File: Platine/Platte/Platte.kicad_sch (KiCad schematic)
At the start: 9 parts, among them J1 Conn_01x07_MountingPin

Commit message: Plate PCB almost done
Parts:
- added J2: Conn_01x08_Socket, symbol Connector:Conn_01x08_Socket
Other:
- note added: "Mec. Stecker"
- note added: "Outputs: clock, amp_data & GNDD"
- note added: "Voltage Input: 3.3V, GNDA"
- note removed: "Outputs (6)"
- note removed: "Voltage Input"
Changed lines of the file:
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@@
+		)
+	)
+	(text "Mec. Stecker"
+		(exclude_from_sim no)
+		(at 73.406 93.726 0)
+		(effects
+			(font
+				(size 1.27 1.27)
+			)
+			(justify left bottom)
 		)
 	)
@@
 		)
 	)
-	(text "Outputs\n(6)"
-		(exclude_from_sim no)
-		(at 49.022 114.808 0)
+	(text "Outputs: clock,\namp_data & GNDD"
+		(exclude_from_sim no)
+		(at 40.132 125.476 0)
 		(effects
 			(font
@@
 		)
 	)
-	(text "Voltage\nInput"
-		(exclude_from_sim no)
-		(at 49.022 105.664 0)
+	(text "Voltage Input: \n3.3V, GNDA"
+		(exclude_from_sim no)
+		(at 45.466 96.266 0)
 		(effects
 			(font
@@
 					(unit 1)
 				)
+			)
+		)
+	)
+	(symbol
+		(lib_id "Connector:Conn_01x08_Socket")
+		(at 81.28 107.95 0)
+		(unit 1)
+		(exclude_from_sim no)
+		(in_bom yes)
+		(on_board yes)
+		(dnp no)
+		(fields_autoplaced yes)
+		(property "Reference" "J2"
+			(at 82.55 107.9499 0)
+			(effects
+				(font
+					(size 1.27 1.27)
+				)
+				(justify left)
+			)
+		)
+		(property "Value" "Conn_01x08_Socket"
+			(at 82.55 110.4899 0)
+			(effects
+				(font
+					(size 1.27 1.27)
+				)
+				(justify left)
+			)
+		)
+		(property "Footprint" ""
+			(at 81.28 107.95 0)
+			(effects
+				(font
+					(size 1.27 1.27)
+				)
+				(hide yes)
+			)
+		)
+		(property "Datasheet" "~"
+			(at 81.28 107.95 0)
+			(effects
+				(font
+					(size 1.27 1.27)
+				)
+				(hide yes)
+			)
+		)
+		(property "Description" "Generic connector, single row, 01x08, script generated"
+			(at 81.28 107.95 0)
+			(effects
+				(font
+					(size 1.27 1.27)
+				)
+				(hide yes)
+			)
+		)
+		(pin "2"
+		)
+		(pin "8"
+		)
+		(pin "4"
+		)
+		(pin "7"
+		)
+		(pin "3"
+		)
+		(pin "1"
+		)
+		(pin "6"
+		)
+		(pin "5"
+		)
+		(instances
+			(project ""
+				(path "/8ec2d373-240e-44f6-ab9e-7e8ab23831f1"
+					(reference "J2")
+					(unit 1)
+				)

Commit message: Few changes plate PCB
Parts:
- removed J1: Conn_01x07_MountingPin, Connector_JST:JST_GH_BM07B-GHS-TBT_1x07-1MP_P1.25mm_Vertical, symbol Connector_Generic_MountingPin:Conn_01x07_MountingPin
- added J1: Conn_01x08_MountingPin, Connector_JST:JST_GH_BM08B-GHS-TBT_1x08-1MP_P1.25mm_Vertical, symbol Connector_Generic_MountingPin:Conn_01x08_MountingPin
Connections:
- net +3.3V: now also J1.2 (Pin_2)
- net GNDA: now also J1.8 (Pin_8)
- net GNDD: now also J1.7 (Pin_7)
- net amp_data1: now also J1.4 (Pin_4)
- net amp_data2: now also J1.5 (Pin_5)
- net amp_data3: now also J1.6 (Pin_6)
- net out_clock: now also J1.3 (Pin_3)
- new net VCC: J1.1 (Pin_1)
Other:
- note added: "+100V"

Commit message: small changes
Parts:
- R1, R2, R3: footprint Resistor_SMD:R_01005_0402Metric_Pad0.57x0.30mm_HandSolder -> Resistor_SMD:R_0201_0603Metric_Pad0.64x0.40mm_HandSolder
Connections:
- net analog_inp_low1 is gone; now on net VCC: R1.1, U1.3 (AIN)
- net analog_inp_low2 is gone; now on net VCC: R2.1, U2.3 (AIN)
- net analog_inp_low3 is gone; now on net VCC: R3.1, U3.3 (AIN)

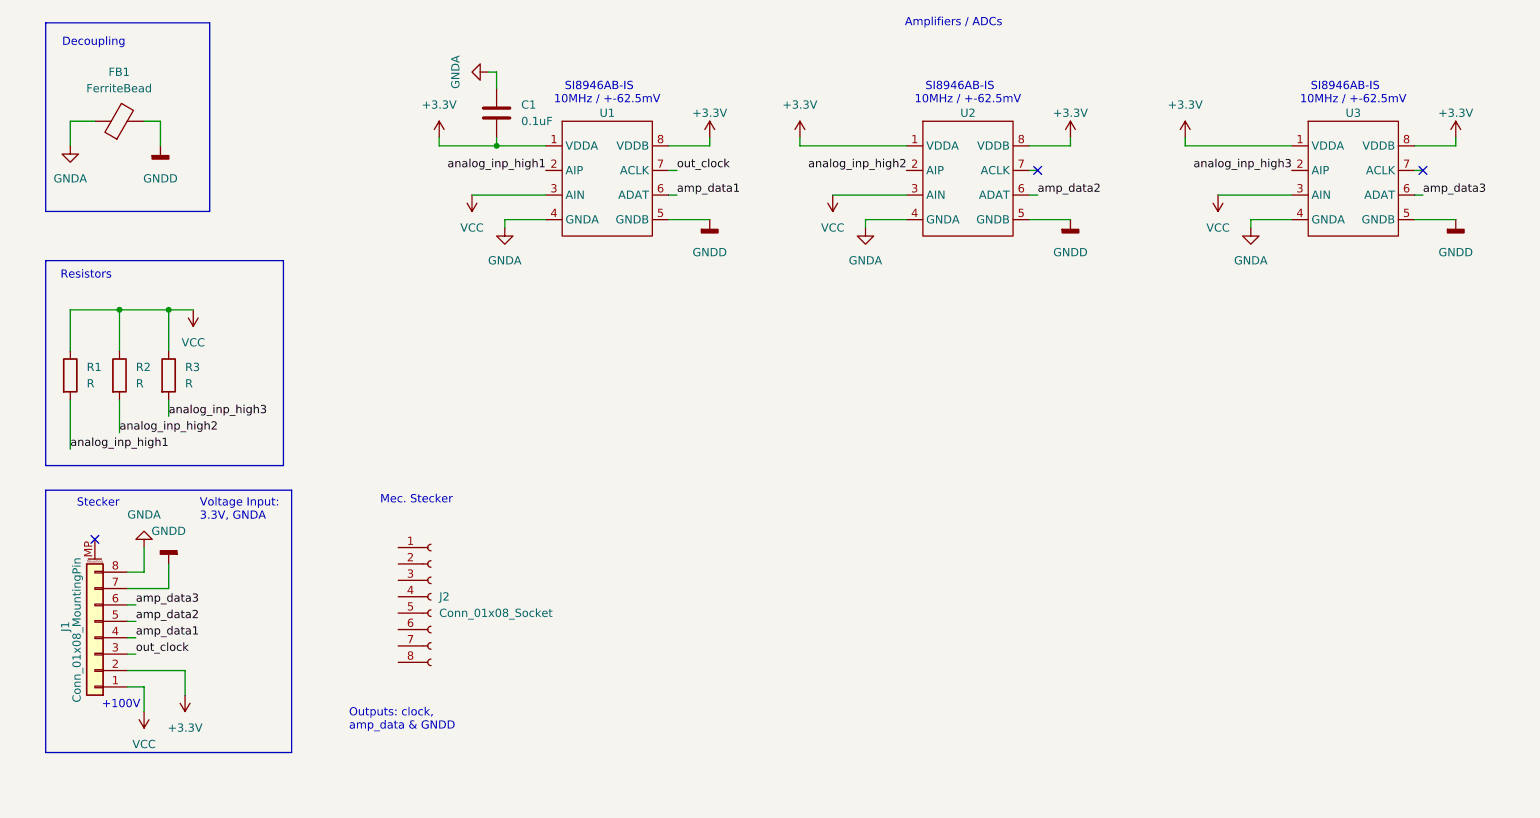
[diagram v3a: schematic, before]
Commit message: Adding now RC filter and DC Converter to Plate PCB
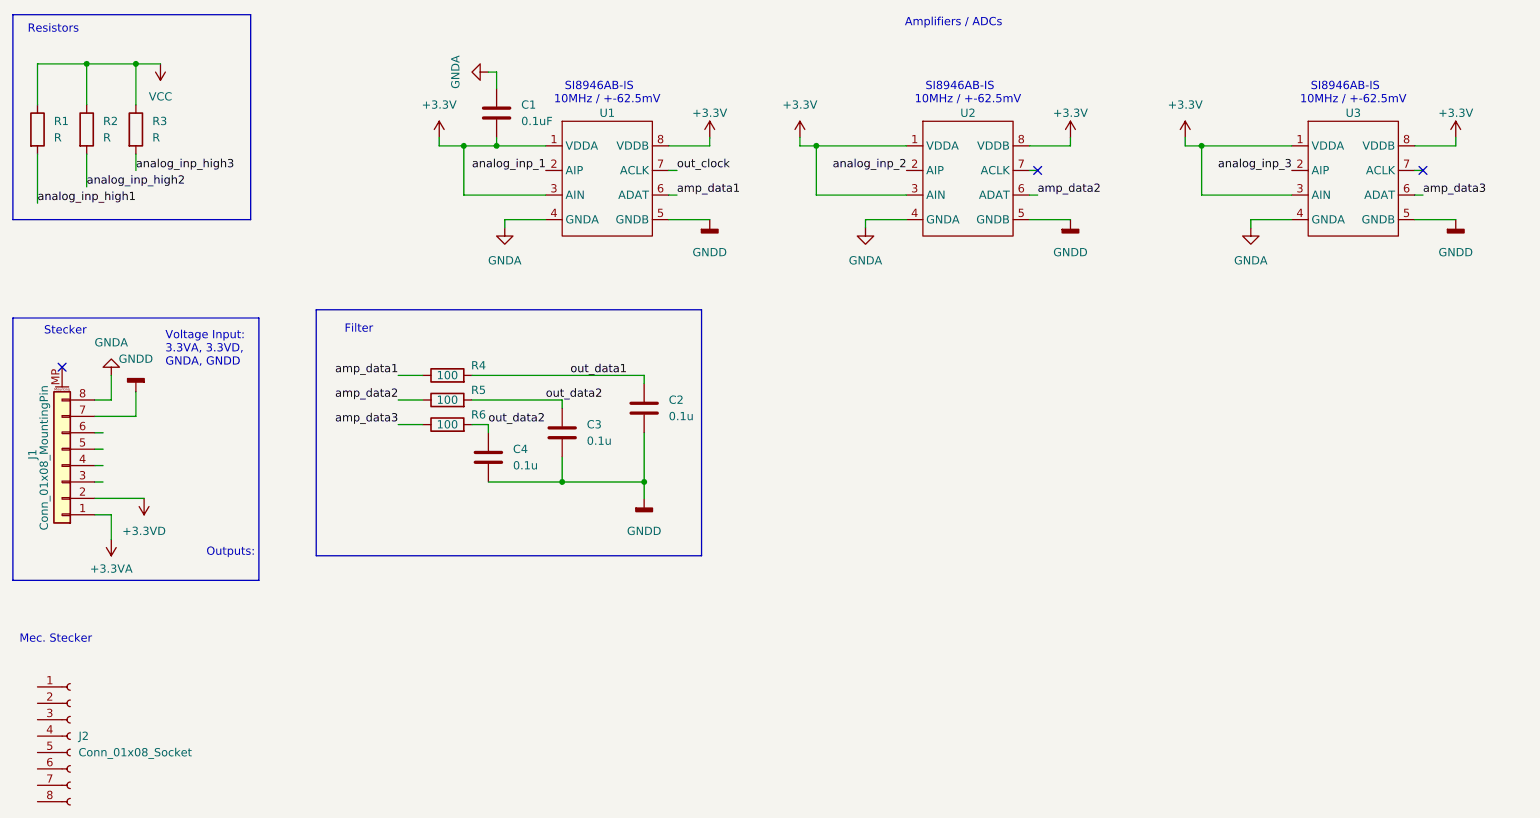
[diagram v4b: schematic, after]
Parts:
- removed FB1: FerriteBead, Inductor_SMD:L_0402_1005Metric_Pad0.77x0.64mm_HandSolder, symbol Device:FerriteBead
- added C2, C3, C4: 0.1u, Capacitor_SMD:C_0201_0603Metric_Pad0.64x0.40mm_HandSolder, symbol Device:C
- added R4, R5, R6: 100, Resistor_SMD:R_0201_0603Metric_Pad0.64x0.40mm_HandSolder, symbol Device:R
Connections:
- net +3.3V: now also U1.3 (AIN), U2.3 (AIN), U3.3 (AIN); no longer J1.2 (Pin_2)
- net GNDD: now also C2.2, C3.1, C4.2
- net VCC: no longer J1.1 (Pin_1), U1.3 (AIN), U2.3 (AIN), U3.3 (AIN)
- net amp_data1: now also R4.1; no longer J1.4 (Pin_4)
- net amp_data2: now also R5.1; no longer J1.5 (Pin_5)
- net amp_data3: now also R6.1; no longer J1.6 (Pin_6)
- net analog_inp_high1: no longer U1.2 (AIP)
- net analog_inp_high2: no longer U2.2 (AIP)
- net analog_inp_high3: no longer U3.2 (AIP)
- net out_clock: no longer J1.3 (Pin_3)
- new net +3.3VA: J1.1 (Pin_1)
- new net +3.3VD: J1.2 (Pin_2)
- new net analog_inp_1: U1.2 (AIP)
- new net analog_inp_2: U2.2 (AIP)
- new net analog_inp_3: U3.2 (AIP)
- new net out_data1: C2.1, R4.2
- new net out_data2: C3.2, C4.1, R5.2, R6.2
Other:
- note added: "Filter"
- note added: "Outputs:"
- note added: "Voltage Input: 3.3VA, 3.3VD, GNDA, GNDD"
- note removed: "+100V"
- note removed: "Decoupling"
- note removed: "Outputs: clock, amp_data & GNDD"
- note removed: "Voltage Input: 3.3V, GNDA"
- moved on the sheet: J1, J2, R1, R2, R3

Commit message: Nothing special
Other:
- added sheet SgnlCond (sgnlcond.kicad_sch)
- note added: "Signal Conditioning"
- note removed: "Filter"
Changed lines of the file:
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@@
 		)
 	)
-	(text "Filter\n"
-		(exclude_from_sim no)
-		(at 70.104 66.548 0)
+	(text "Signal Conditioning\n"
+		(exclude_from_sim no)
+		(at 74.168 67.056 0)
 		(effects
 			(font
@@
 				)
 			)
+		)
+	)
+	(sheet
+		(at 190.5 95.25)
+		(size 17.78 20.32)
+		(fields_autoplaced yes)
+		(stroke
+			(width 0.1524)
+			(type solid)
+		)
+		(fill
+			(color 0 0 0 0.0000)
+		)
+		(property "Sheetname" "SgnlCond"
+			(at 190.5 94.5384 0)
+			(effects
+				(font
+					(size 1.27 1.27)
+				)
+				(justify left bottom)
+			)
+		)
+		(property "Sheetfile" "sgnlcond.kicad_sch"
+			(at 190.5 116.1546 0)
+			(effects
+				(font
+					(size 1.27 1.27)
+				)
+				(justify left top)
+			)
+		)
+		(instances
+			(project "Platte"
+				(path "/8ec2d373-240e-44f6-ab9e-7e8ab23831f1"
+					(page "2")
+				)
+			)

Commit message: ok
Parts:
- removed C2, C3, C4: 0.1u, Capacitor_SMD:C_0201_0603Metric_Pad0.64x0.40mm_HandSolder, symbol Device:C
- removed R4, R5, R6: 100, Resistor_SMD:R_0201_0603Metric_Pad0.64x0.40mm_HandSolder, symbol Device:R
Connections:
- net VCC is gone; now on net +3.3V: R1.1, R2.1, R3.1
- net analog_inp_high1 is gone; now on net analog_inp_1: R1.2
- net analog_inp_high2 is gone; now on net analog_inp_2: R2.2
- net analog_inp_high3 is gone; now on net analog_inp_3: R3.2
- net +3.3V: no longer U1.8 (VDDB), U2.8 (VDDB), U3.8 (VDDB)
- net +3.3VA: now also U1.8 (VDDB), U2.8 (VDDB), U3.8 (VDDB)
- net out_clock: no longer names the net of U1.7 (ACLK)
- no-connect marks 3 -> 4

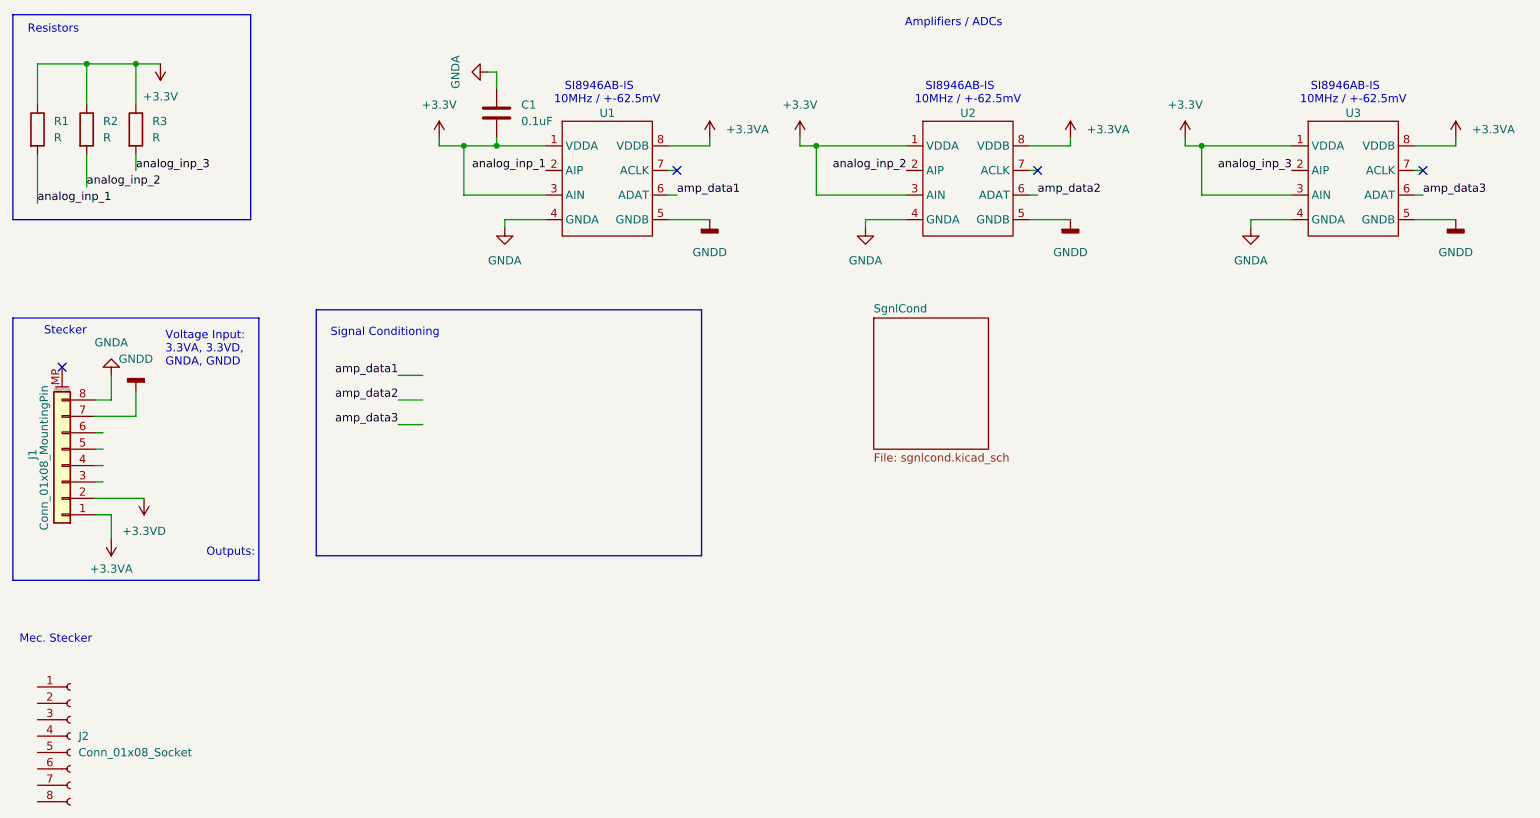
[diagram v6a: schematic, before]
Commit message: plate pcb almost finished
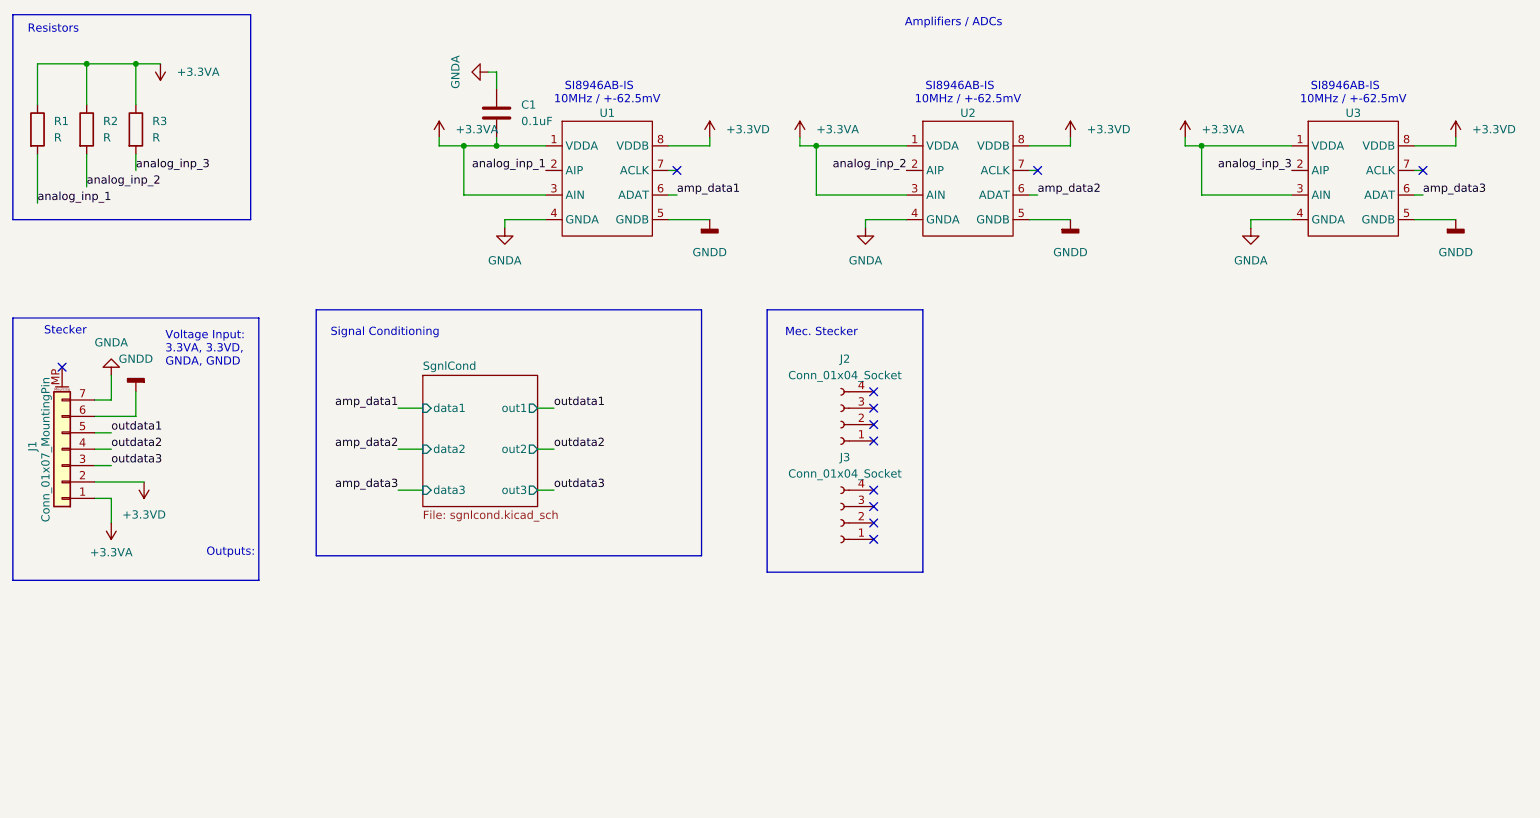
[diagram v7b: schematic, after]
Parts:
- removed J1: Conn_01x08_MountingPin, Connector_JST:JST_GH_BM08B-GHS-TBT_1x08-1MP_P1.25mm_Vertical, symbol Connector_Generic_MountingPin:Conn_01x08_MountingPin
- removed J2: Conn_01x08_Socket, symbol Connector:Conn_01x08_Socket
- added J1: Conn_01x07_MountingPin, Connector_JST:JST_GH_BM07B-GHS-TBT_1x07-1MP_P1.25mm_Vertical, symbol Connector_Generic_MountingPin:Conn_01x07_MountingPin
- added J2, J3: Conn_01x04_Socket, Connector_PinHeader_1.27mm:PinHeader_1x04_P1.27mm_Vertical, symbol Connector:Conn_01x04_Socket
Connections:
- net +3.3V is gone; now on net +3.3VA: C1.2, R1.1, R2.1, R3.1, U1.1 (VDDA), U1.3 (AIN), U2.1 (VDDA), U2.3 (AIN), U3.1 (VDDA), U3.3 (AIN)
- net +3.3VA: now also J1.1 (Pin_1); no longer U1.8 (VDDB), U2.8 (VDDB), U3.8 (VDDB)
- net +3.3VD: now also U1.8 (VDDB), U2.8 (VDDB), U3.8 (VDDB), J1.2 (Pin_2)
- net GNDA: now also J1.7 (Pin_7)
- net GNDD: now also J1.6 (Pin_6)
- new net outdata1: J1.5 (Pin_5)
- new net outdata2: J1.4 (Pin_4)
- new net outdata3: J1.3 (Pin_3)
- no-connect marks 4 -> 12
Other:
- sheet SgnlCond ports: added data1, data2, data3, out1, out2, out3; removed none

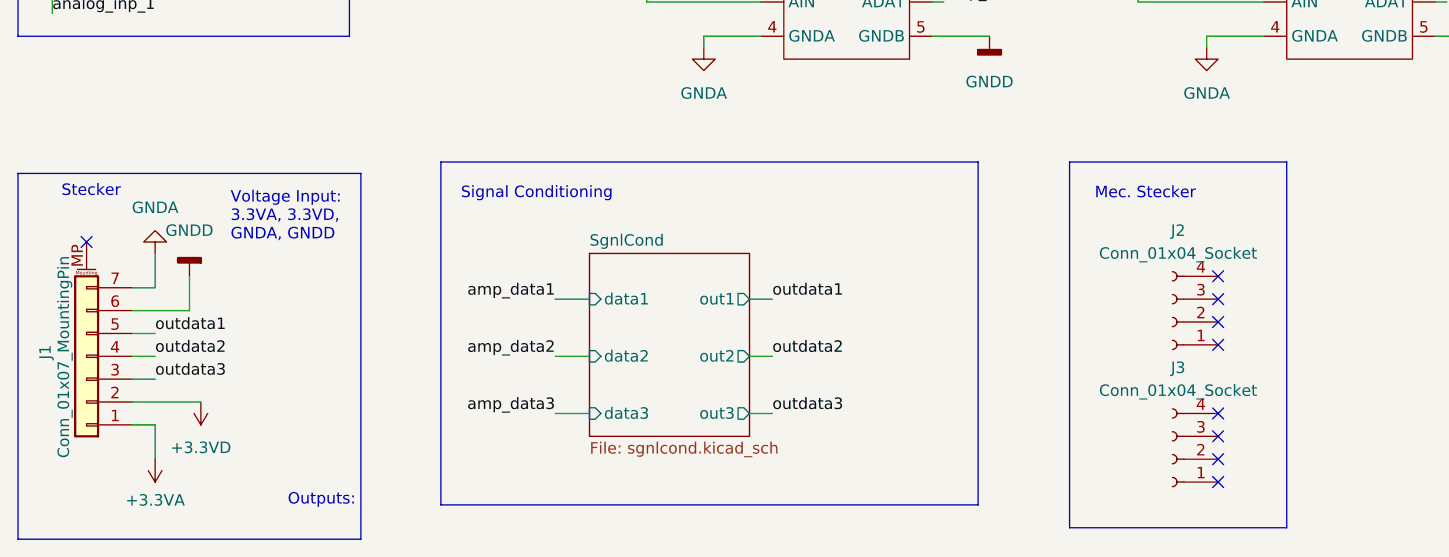
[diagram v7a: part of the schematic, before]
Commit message: Removing CST simulations because of weight, theyre now in the folder outside the repo
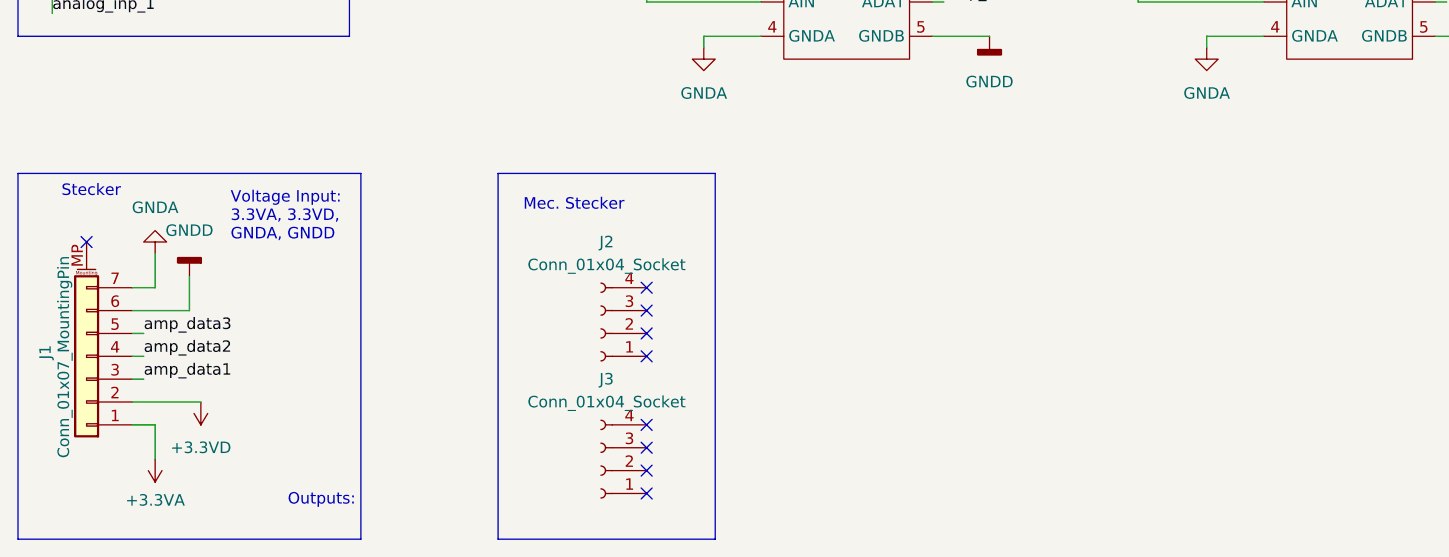
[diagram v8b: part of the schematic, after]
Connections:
- net outdata1 is gone; now on net amp_data3: J1.5 (Pin_5)
- net outdata2 is gone; now on net amp_data2: J1.4 (Pin_4)
- net outdata3 is gone; now on net amp_data1: J1.3 (Pin_3)
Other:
- removed sheet SgnlCond
- note removed: "Signal Conditioning"
- moved on the sheet: J2, J3
